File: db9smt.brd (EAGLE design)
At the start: 31.3 x 16.3 mm, 20 parts, among them CON1 PADONPRINT, CON2 PADONPRINT, CON3 PADONPRINT, CON4 PADONPRINT, CON5 PADONPRINT, CON6 PADONPRINT, CON7 PADONPRINT, CON8 PADONPRINT, CON9 PADONPRINT

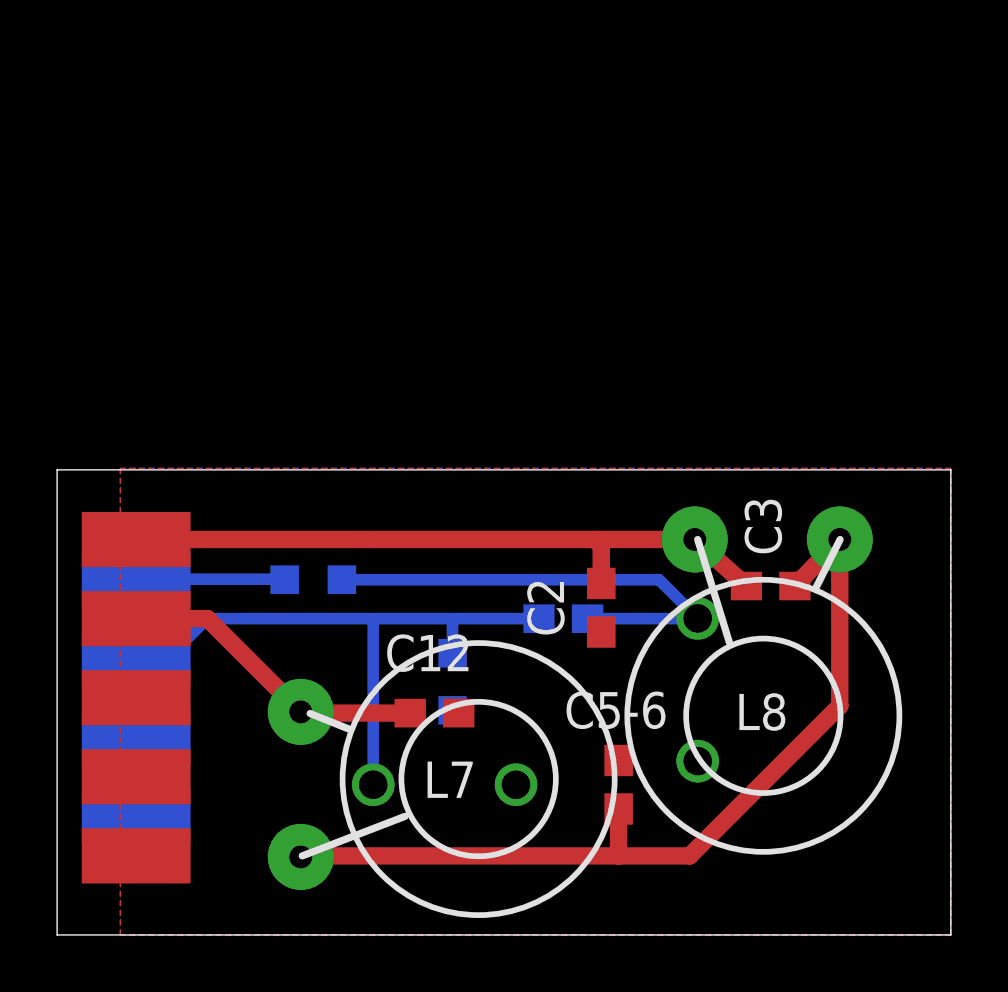
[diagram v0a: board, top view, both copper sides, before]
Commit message: GND between signals, remove note space on backside
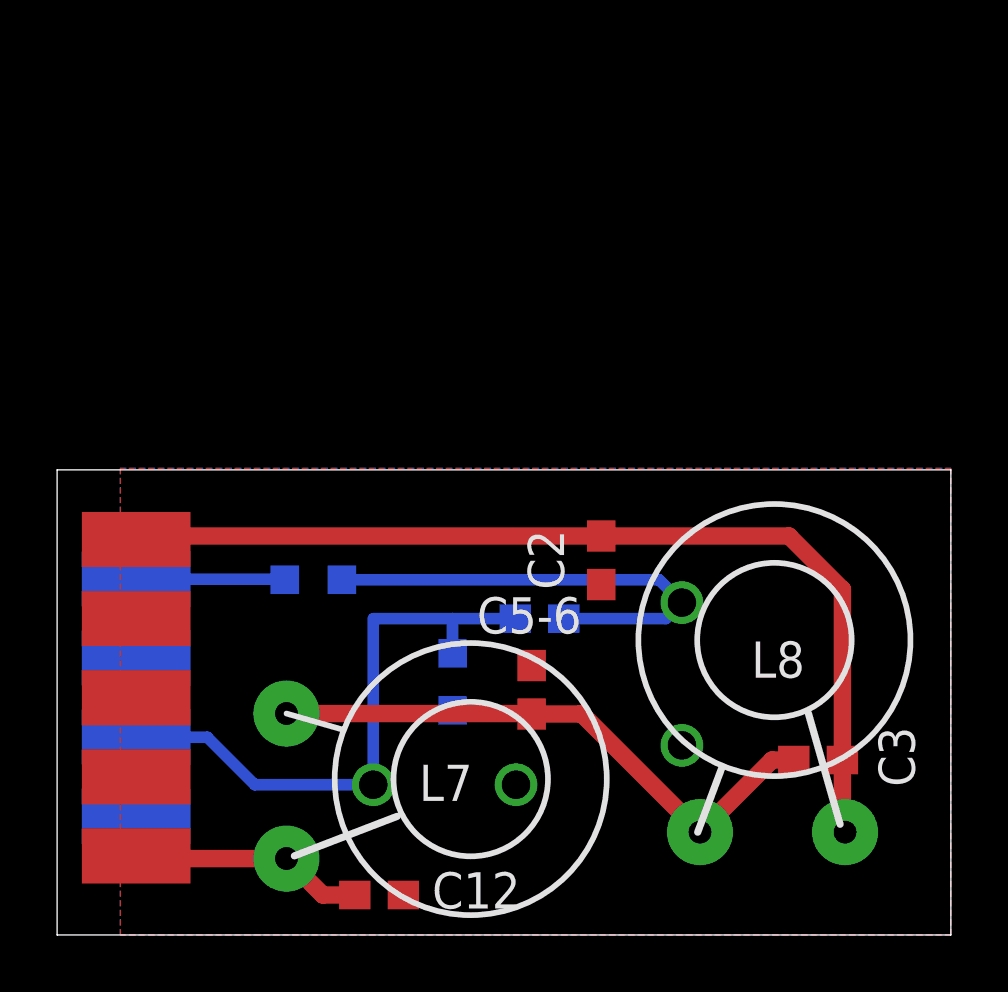
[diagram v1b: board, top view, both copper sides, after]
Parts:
- moved L8 11.5 mm to (27.6, 3.60), turned to 180 degrees
- moved C12 6.66 mm to (11.3, 1.40)
- moved C3 6.32 mm to (26.7, 6.13), turned to 180 degrees
- moved L7 5.05 mm to (8.03, 7.76), turned to 270 degrees
- moved C5-6 4.51 mm to (16.6, 8.59)
- moved C2 1.66 mm to (19.1, 13.1)
- moved C31 0.83 mm to (16.9, 11.1)
- moved CT1 0.78 mm to (21.9, 9.14)
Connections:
- net GND: now also CON2.P$1, CON4.P$1, CON7.P$1, CON9.P$1; no longer CON8.P$1
- net N$1: now also CON8.P$1; no longer CON7.P$1
- net N$5: now also CON5.P$1; no longer CON2.P$1
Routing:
- net N$4: track 23.6 -> 34.3 mm
- net N$6: track 30.8 -> 20.6 mm
- net N$5: track 11.0 -> 8.36 mm
- net N$1: track 21.8 -> 21.0 mm

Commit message: Removed right angle
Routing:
- net N$1: track 21.0 -> 20.0 mm
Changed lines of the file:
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@@
 <contactref element="C31" pad="2"/>
 <contactref element="L4" pad="1"/>
-<wire x1="13.85" y1="11.08" x2="16.047" y2="11.08" width="0.4064" layer="16"/>
-<wire x1="11.08" y1="11.08" x2="13.85" y2="11.08" width="0.4064" layer="16"/>
+<wire x1="16.047" y1="11.08" x2="13.85" y2="11.08" width="0.4064" layer="16"/>
 <wire x1="13.85" y1="9.864" x2="13.85" y2="11.08" width="0.4064" layer="16"/>
-<wire x1="11.073" y1="11.073" x2="11.073" y2="5.263" width="0.4064" layer="16"/>
-<wire x1="11.073" y1="11.073" x2="11.08" y2="11.08" width="0.254" layer="16"/>
+<wire x1="11.073" y1="9.418" x2="11.073" y2="11.073" width="0" layer="19" extent="1-16"/>
+<wire x1="11.073" y1="9.418" x2="11.073" y2="5.263" width="0.4064" layer="16"/>
+<wire x1="11.073" y1="11.073" x2="11.08" y2="11.08" width="0" layer="19" extent="1-16"/>
 <wire x1="11.073" y1="5.263" x2="6.925" y2="5.263" width="0.4064" layer="16"/>
 <contactref element="CON8" pad="P$1"/>
 <wire x1="6.925" y1="5.263" x2="5.263" y2="6.925" width="0.4064" layer="16"/>
 <wire x1="5.263" y1="6.925" x2="2.77" y2="6.925" width="0.4064" layer="16"/>
+<wire x1="13.85" y1="11.08" x2="12.735" y2="11.08" width="0.4064" layer="16"/>
+<wire x1="12.735" y1="11.08" x2="11.073" y2="9.418" width="0.4064" layer="16"/>
 </signal>
 </signals>

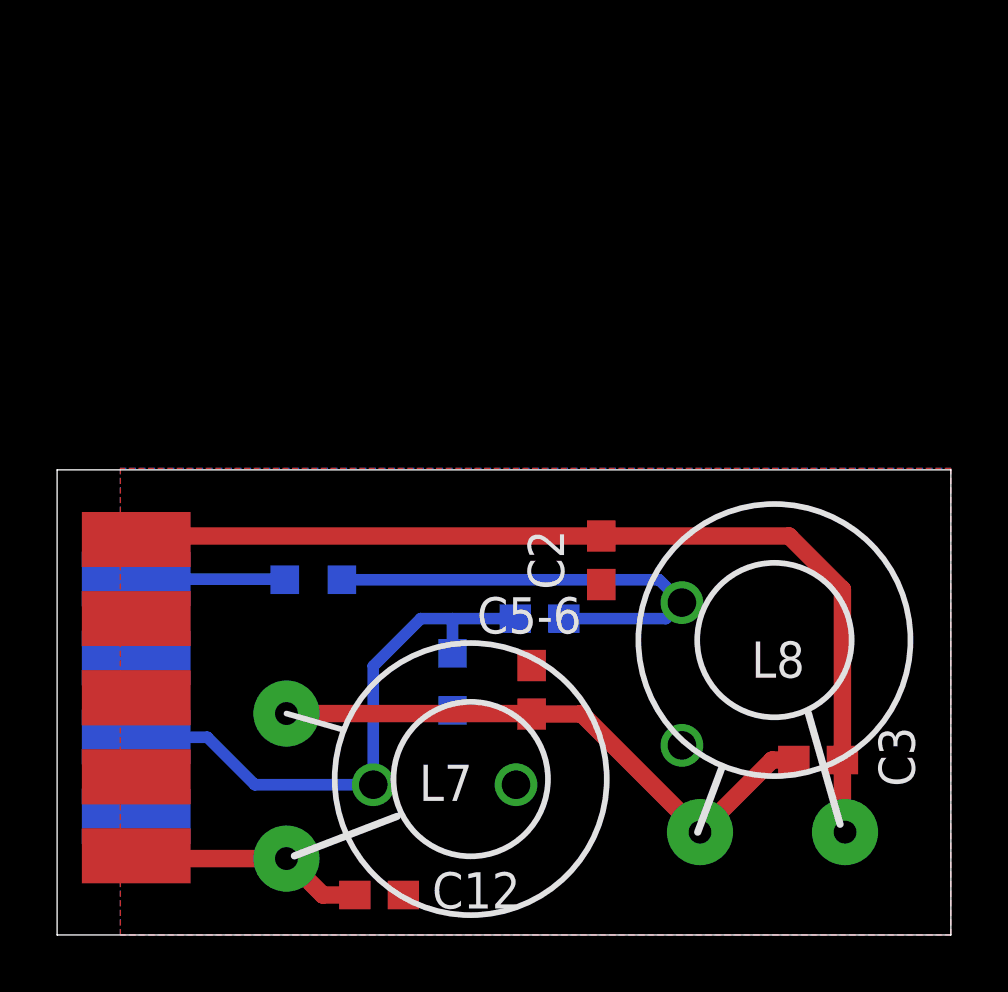
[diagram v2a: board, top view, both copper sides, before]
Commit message: Make DB9 horizontal for smaller footprint and shorter traces
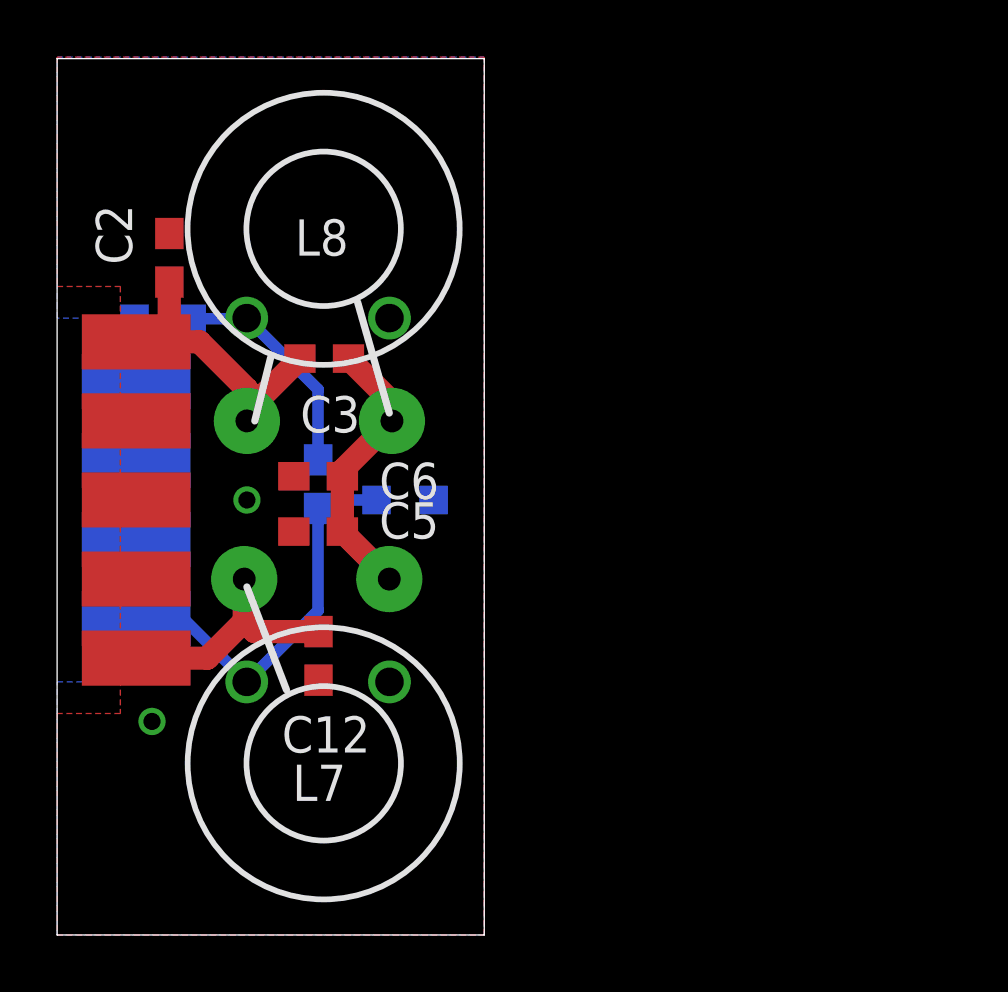
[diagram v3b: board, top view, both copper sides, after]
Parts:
- removed C5-6: 330p, eagle-ltspice:C0603
- added C5, C6: 330p, eagle-ltspice:C0603
- moved L8 25.4 mm to (6.65, 18.0), turned to 0 degrees
- moved C3 22.3 mm to (9.36, 20.2), turned to 0 degrees
- moved C2 18.5 mm to (3.93, 23.7), turned to 90 degrees
- moved CT1 17.8 mm to (9.14, 21.6), turned to 90 degrees
- moved L3 10.5 mm to (3.71, 21.6)
- moved C31 9.07 mm to (9.14, 15.8), turned to 270 degrees
- moved C12 8.64 mm to (9.16, 9.78), turned to 270 degrees
- moved CON5 6.93 mm to (2.77, 9.70)
- moved CON6 6.93 mm to (2.77, 19.4)
- moved CON7 6.93 mm to (2.77, 16.6)
- moved CON4 6.92 mm to (2.77, 12.5)
- moved CON8 6.92 mm to (2.77, 13.8)
- moved CON9 6.92 mm to (2.77, 11.1)
- moved CON1 6.92 mm to (2.77, 20.8)
- moved CON2 6.92 mm to (2.77, 18.0)
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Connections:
- net GND: now also C5.2, C6.2, CON8.P$1; no longer C5-6.2, CON9.P$1
- net N$1: now also CON9.P$1; no longer CON8.P$1
- net N$6: now also C5.1, C6.1; no longer C5-6.1
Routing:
- net N$4: track 34.3 -> 12.0 mm
- net N$6: track 20.6 -> 9.75 mm
- net N$2: track 16.6 -> 7.94 mm
- net N$1: track 20.0 -> 14.1 mm
- net N$3: track 5.21 -> 2.22 mm
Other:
- board size 31.3 x 16.3 mm -> 15 x 30.7 mm

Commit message: Move TX lines on DB9 connector
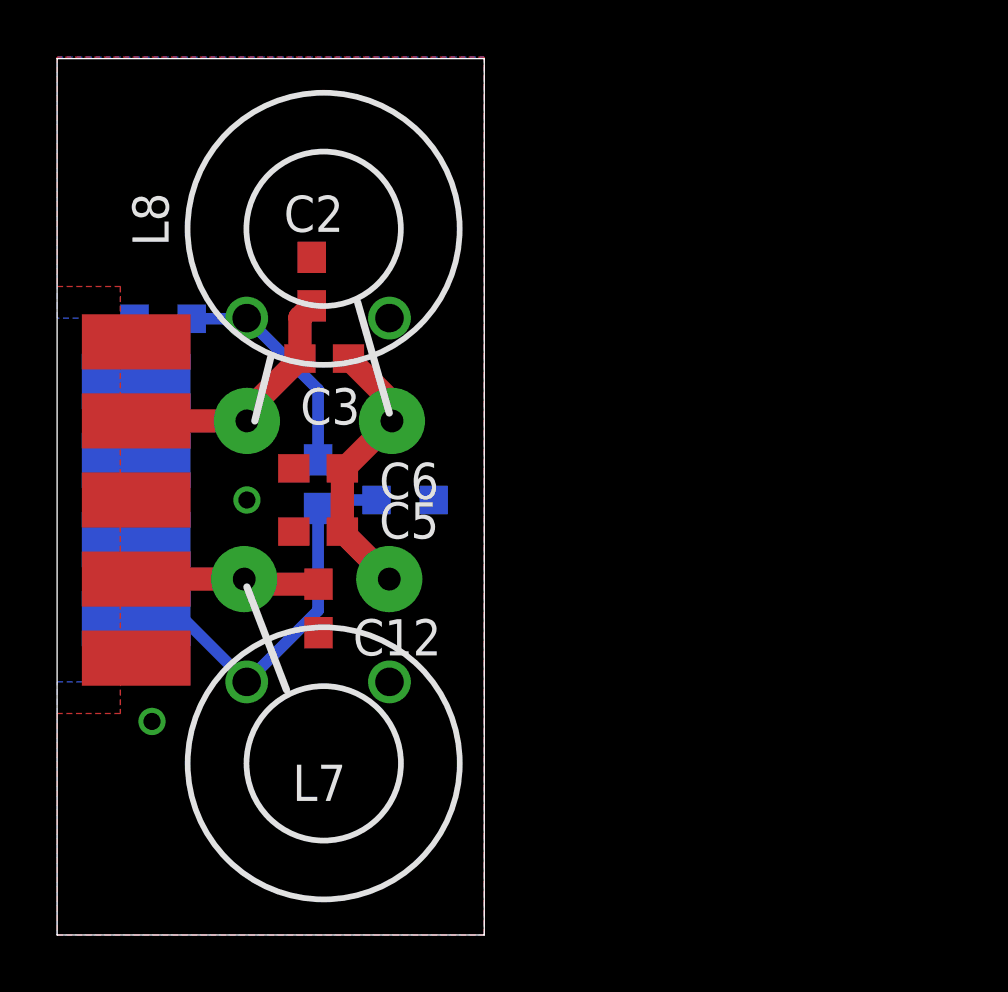
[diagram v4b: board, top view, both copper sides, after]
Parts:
- moved C2 5.05 mm to (8.92, 22.9)
- moved C12 1.66 mm to (9.16, 11.4)
- moved C6 0.28 mm to (9.14, 16.3)
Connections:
- net GND: now also CON1.P$1, CON5.P$1; no longer CON2.P$1, CON4.P$1
- net N$4: now also CON2.P$1; no longer CON1.P$1
- net N$5: now also CON4.P$1; no longer CON5.P$1
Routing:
- net N$4: track 12.0 -> 8.85 mm
- net N$5: track 8.68 -> 6.60 mm

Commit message: Minor fix DB9SMT
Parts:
- moved C12 0.62 mm to (8.60, 11.2)
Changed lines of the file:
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@@
 <attribute name="SPICEPREFIX" value="C" x="8.917" y="22.886" size="1.778" layer="27" rot="R90" display="off"/>
 </element>
-<element name="C12" library="eagle-ltspice" package="C0603" value="150p" x="9.156" y="11.437" smashed="yes" rot="R270">
-<attribute name="NAME" x="10.365" y="9.791" size="1.27" layer="25"/>
-<attribute name="SPICEMODEL" value="NONE" x="9.156" y="11.437" size="1.778" layer="27" rot="R270" display="off"/>
-<attribute name="SPICEPREFIX" value="C" x="9.156" y="11.437" size="1.778" layer="27" rot="R270" display="off"/>
+<element name="C12" library="eagle-ltspice" package="C0603" value="150p" x="8.602" y="11.16" smashed="yes" rot="R270">
+<attribute name="NAME" x="9.811" y="9.791" size="1.27" layer="25"/>
+<attribute name="SPICEMODEL" value="NONE" x="8.602" y="11.16" size="1.778" layer="27" rot="R270" display="off"/>
+<attribute name="SPICEPREFIX" value="C" x="8.602" y="11.16" size="1.778" layer="27" rot="R270" display="off"/>
 </element>
 <element name="C6" library="eagle-ltspice" package="C0603" value="330p" x="9.141" y="16.343" smashed="yes" rot="R180">
@@
 <contactref element="CON5" pad="P$1"/>
 <contactref element="CON1" pad="P$1"/>
-<wire x1="9.156" y1="10.587" x2="8.291" y2="14.127" width="0" layer="19" extent="1-1"/>
 </signal>
 <signal name="N$2">
@@
 <wire x1="6.554" y1="12.465" x2="6.653" y2="12.564" width="0.8128" layer="1"/>
 <wire x1="6.554" y1="12.465" x2="6.732" y2="12.287" width="0.8128" layer="1"/>
-<wire x1="6.732" y1="12.287" x2="9.156" y2="12.287" width="0.8128" layer="1"/>
+<wire x1="6.554" y1="12.465" x2="7.009" y2="12.01" width="0.8128" layer="1"/>
+<wire x1="7.009" y1="12.01" x2="8.602" y2="12.01" width="0.8128" layer="1"/>
 </signal>
 <signal name="N$6">
